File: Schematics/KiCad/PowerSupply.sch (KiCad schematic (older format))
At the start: 7 parts

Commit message: Replace PowerSupply.sch
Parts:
- removed Microphone1: ADMP504ACEZ-RL, PiHAT_Power_Supply:ADMP504ACEZ-RL, symbol PiHAT_Power_Supply-rescue:ADMP504ACEZ-RL-2021-06-02_12-37-56
- added MIC?: ICS-40212, ICS-40212_IVS, symbol new_microphone:ICS-40212
- C1: symbol PiHAT_Power_Supply-rescue:LMK107BBJ226MA-T-2021-06-02_13-25-42 -> 2021-06-02_13-25-42:LMK107BBJ226MA-T
- D1: symbol PiHAT_Power_Supply-rescue:1N914-Diode -> Diode:1N914
- L1: symbol PiHAT_Power_Supply-rescue:B82464A4474K000-2021-06-02_13-47-42 -> 2021-06-02_13-47-42:B82464A4474K000
- NMOS1: symbol PiHAT_Power_Supply-rescue:FDW2503NZ-2021-06-02_13-00-23 -> 2021-06-02_13-00-23:FDW2503NZ
- R1: symbol PiHAT_Power_Supply-rescue:R-Device -> pspice:R
- R2: symbol PiHAT_Power_Supply-rescue:R-Device -> Device:R
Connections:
- wire segments 31 -> 34
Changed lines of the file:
@@
 $EndDescr
 $Comp
-L PiHAT_Power_Supply-rescue:R-Device R2
+L Device:R R2
 U 1 1 60B8698F
 P 6950 4200
@@
 $EndComp
 $Comp
-L PiHAT_Power_Supply-rescue:1N914-Diode D1
+L Diode:1N914 D1
 U 1 1 60B8E4ED
 P 4400 3800
@@
 $EndComp
 $Comp
-L PiHAT_Power_Supply-rescue:R-Device R1
+L pspice:R R1
 U 1 1 60B86505
 P 3150 4000
@@
 Text GLabel 1500 3750 0    71   Input ~ 0
 5V
-$Comp
-L PiHAT_Power_Supply-rescue:ADMP504ACEZ-RL-2021-06-02_12-37-56 Microphone1
-U 1 1 60B9E2AA
-P 7650 3250
-F 0 "Microphone1" H 8850 3637 60  0000 C CNN
-F 1 "ADMP504ACEZ-RL" H 8850 3531 60  0000 C CNN
-F 2 "PiHAT_Power_Supply:ADMP504ACEZ-RL" H 8850 3490 60  0001 C CNN
-F 3 "" H 7650 3250 60  0000 C CNN
-	1    7650 3250
-	1    0    0    -1
-$EndComp
 Wire Wire Line
 	7400 2900 7400 3250
 Wire Wire Line
-	7400 3250 7650 3250
-Wire Wire Line
-	10050 3450 10050 5500
-Wire Wire Line
-	10050 5500 6950 5500
+	10050 5500 7950 5500
 Wire Wire Line
 	4400 2900 4400 3650
@@
 Wire Wire Line
 	6950 5500 5800 5500
-Text GLabel 8350 4400 2    71   Input ~ 0
+Text GLabel 9850 2700 2    71   Input ~ 0
 Vmic
-Wire Wire Line
-	7650 3450 7650 4400
-Wire Wire Line
-	7650 4400 8350 4400
 $Comp
-L PiHAT_Power_Supply-rescue:GND-power #PWR0101
+L power:GND #PWR0101
 U 1 1 60BA54EE
 P 5100 5950
@@
 Connection ~ 7400 2900
 $Comp
-L PiHAT_Power_Supply-rescue:FDW2503NZ-2021-06-02_13-00-23 NMOS1
+L 2021-06-02_13-00-23:FDW2503NZ NMOS1
 U 1 1 60BA8A9A
 P 3150 1100
@@
 Power supply: 5V-2V buck regulator\nUsed to drive microphone and op-amp.
 $Comp
-L PiHAT_Power_Supply-rescue:LMK107BBJ226MA-T-2021-06-02_13-25-42 C1
+L 2021-06-02_13-25-42:LMK107BBJ226MA-T C1
 U 1 1 60BB3CDF
 P 5800 4000
@@
 $EndComp
 $Comp
-L PiHAT_Power_Supply-rescue:B82464A4474K000-2021-06-02_13-47-42 L1
+L 2021-06-02_13-47-42:B82464A4474K000 L1
 U 1 1 60BB6AF3
 P 4900 2900
@@
 	6950 2900 7400 2900
 Wire Wire Line
-	2850 1100 2950 1100
-Wire Wire Line
-	2950 1100 3050 1100
-Connection ~ 2950 1100
-Connection ~ 3050 1100
-Wire Wire Line
-	3050 1100 3150 1100
-Wire Wire Line
 	3150 4150 3150 4800
 Wire Wire Line
 	1500 2900 1500 3750
+Wire Wire Line
+	2850 1100 3150 1100
+$Comp
+L new_microphone:ICS-40212 MIC?
+U 1 1 60C0CF1F
+P 9550 3150
+F 0 "MIC?" H 10350 3537 60  0000 C CNN
+F 1 "ICS-40212" H 10350 3431 60  0000 C CNN
+F 2 "ICS-40212_IVS" H 10350 3390 60  0001 C CNN
+F 3 "" H 9550 3150 60  0000 C CNN
+	1    9550 3150
+	-1   0    0    -1
+$EndComp
+Wire Wire Line
+	7400 3250 7950 3250
+Wire Wire Line
+	7950 3350 7950 5500
+Connection ~ 7950 5500
+Wire Wire Line
+	7950 5500 6950 5500
+Wire Wire Line
+	9550 3250 10050 3250
+Wire Wire Line
+	10050 3250 10050 3350
+Wire Wire Line
+	9550 3350 10050 3350
+Connection ~ 10050 3350
+Wire Wire Line
+	10050 3350 10050 5500
+Wire Wire Line
+	9550 3150 9550 2700
+Wire Wire Line
+	9550 2700 9850 2700
 $EndSCHEMATC

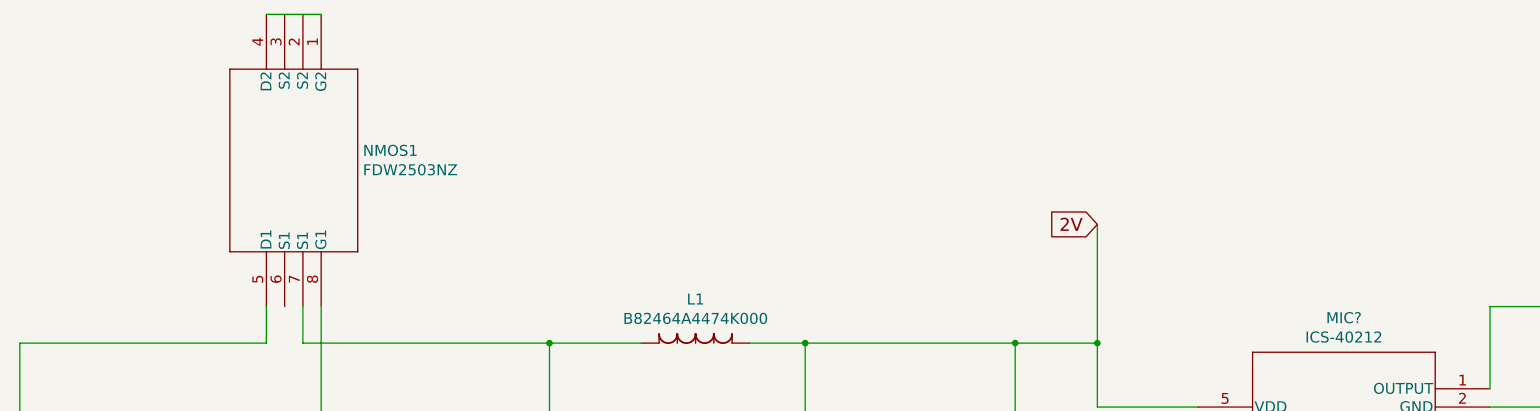
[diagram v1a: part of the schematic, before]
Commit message: Replace PowerSupply.sch
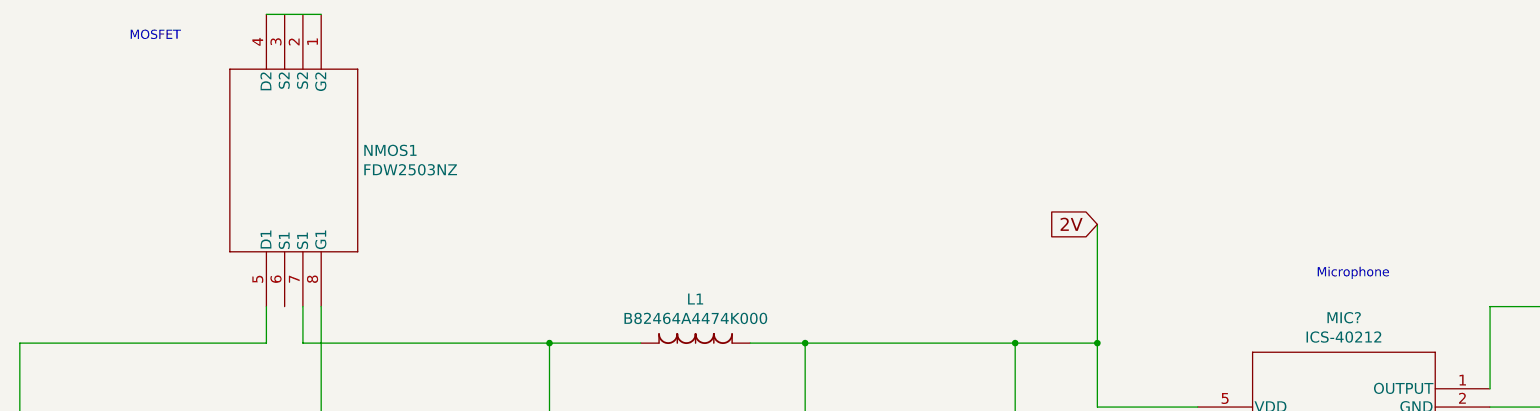
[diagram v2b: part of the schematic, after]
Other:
- note added: "MOSFET"
- note added: "Microphone"
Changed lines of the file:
@@
 Wire Wire Line
 	9550 2700 9850 2700
+Text Notes 2100 1250 0    50   ~ 0
+MOSFET
+Text Notes 8600 2550 0    50   ~ 0
+Microphone
 $EndSCHEMATC
